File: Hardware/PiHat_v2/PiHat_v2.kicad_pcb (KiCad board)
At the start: 2 copper layers, 64 x 55 mm, 0 parts

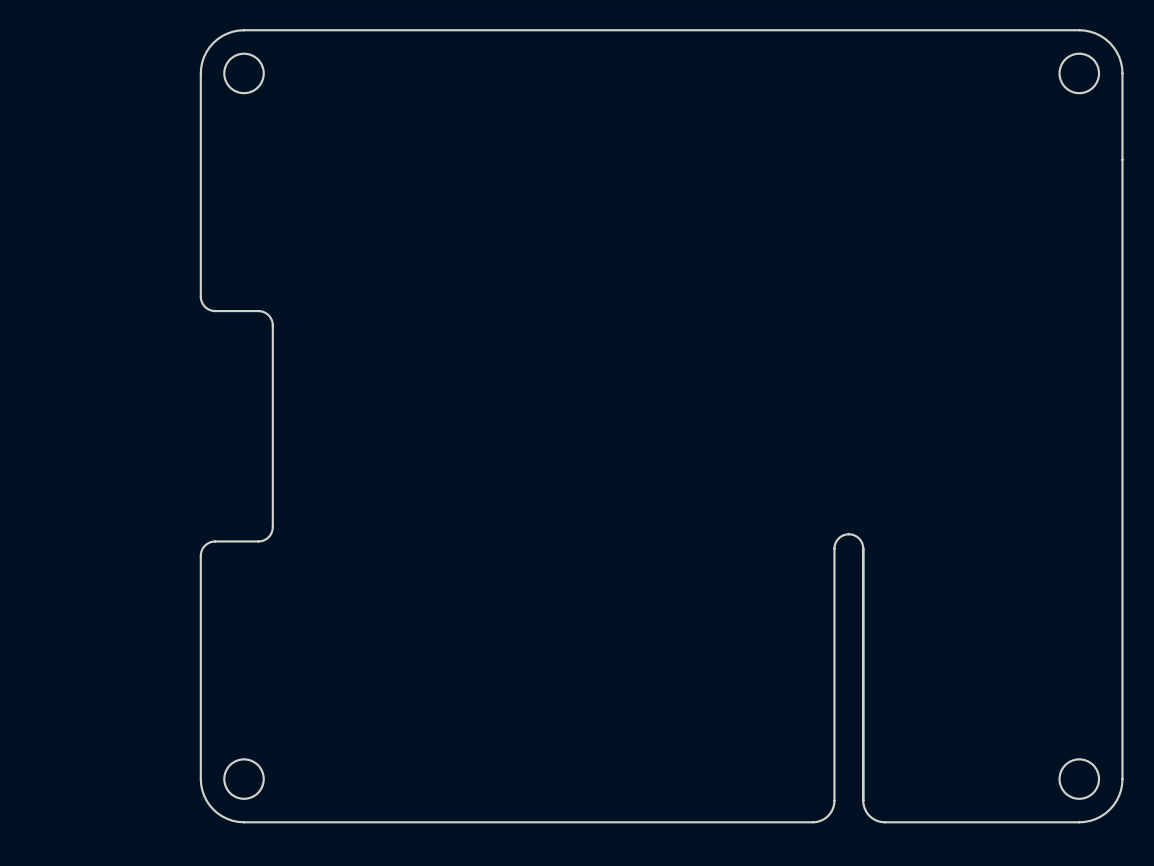
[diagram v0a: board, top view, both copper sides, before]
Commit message: Correct EEPROM Schematic - Add Pin Numbers
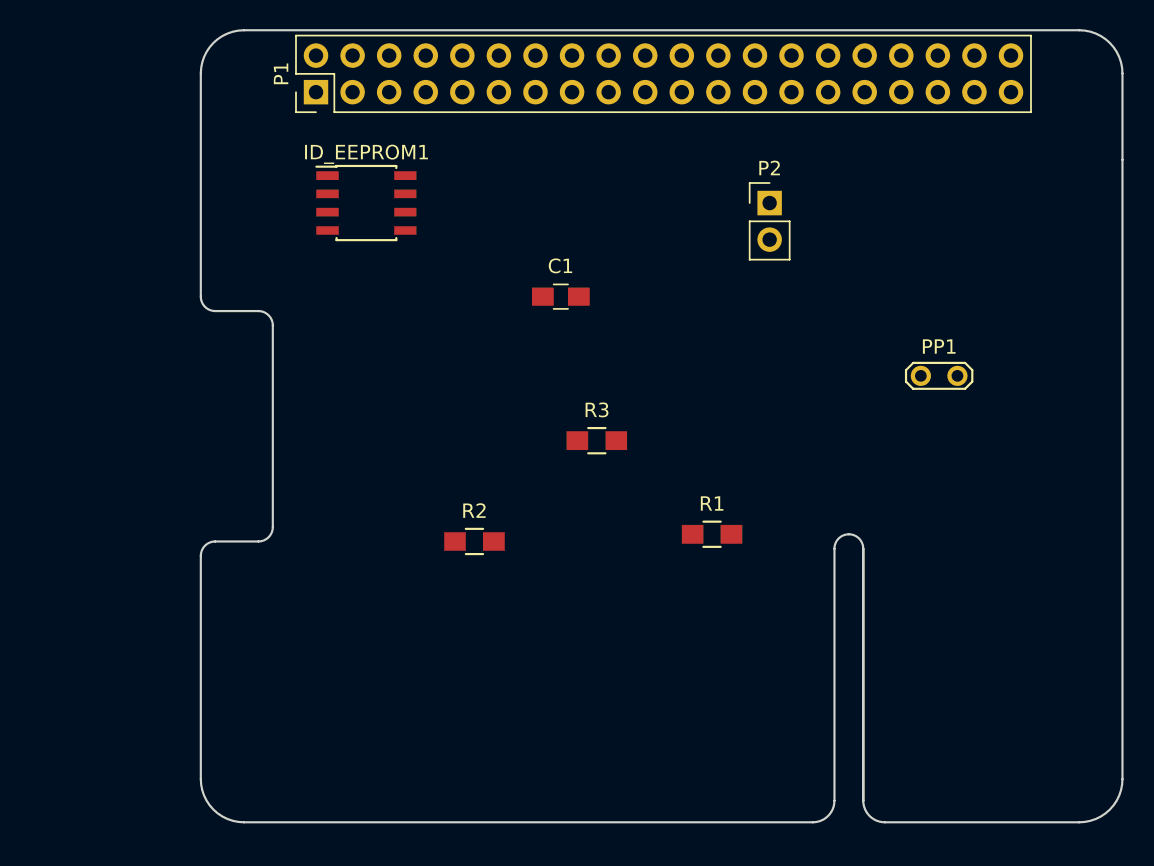
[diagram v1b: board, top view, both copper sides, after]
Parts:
- added C1: 100n, Capacitors_SMD:C_0805_HandSoldering, F.Cu at (119.0, 80.5)
- added ID_EEPROM1: CAT24C32, Housings_SOIC:SOIC-8_3.9x4.9mm_Pitch1.27mm, F.Cu at (105.5, 74.0)
- added P1: CONN_02X20, Pin_Headers:Pin_Header_Straight_2x20_Pitch2.54mm, F.Cu at (102.0, 66.3)
- added P2: CONN_01X02, Pin_Headers:Pin_Header_Straight_1x02_Pitch2.54mm, F.Cu at (133.5, 74.0)
- added PP1: horizTest, Measurement_Points:Test_Point_2Pads, F.Cu at (144.0, 86.0)
- added R1: 1K, Resistors_SMD:R_0805_HandSoldering, F.Cu at (129.5, 97.0)
- added R2: 3.9K, Resistors_SMD:R_0805_HandSoldering, F.Cu at (113.0, 97.5)
- added R3: 3.9K, Resistors_SMD:R_0805_HandSoldering, F.Cu at (121.5, 90.5)
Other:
- outline, holes or cut-outs redrawn

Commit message: Rough Sketch of Schematic and all Footprints Complete
* I've completed a first draft of the schematic, and verified that all
parts have a footprint.
* Next steps include routing the PCB, verifying the designs, and
including any changes.
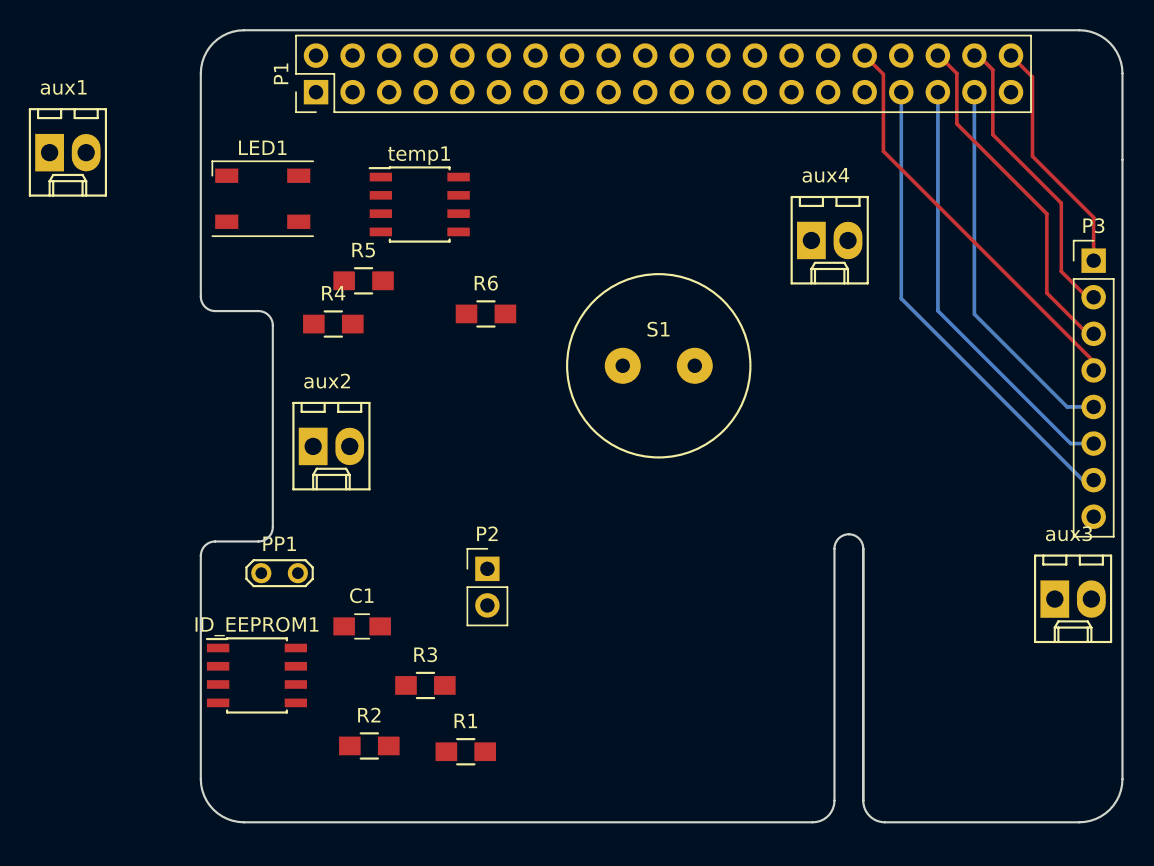
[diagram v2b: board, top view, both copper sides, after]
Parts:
- added LED1: Led_RGB_CA, LEDs:LED_Cree-PLCC4, F.Cu at (98.3, 73.7)
- added P3: CONN_01X08, Pin_Headers:Pin_Header_Straight_1x08_Pitch2.54mm, F.Cu at (156.0, 78.0)
- added R4: R, Resistors_SMD:R_0805_HandSoldering, F.Cu at (103.2, 82.4)
- added R5: R, Resistors_SMD:R_0805_HandSoldering, F.Cu at (105.3, 79.4)
- added R6: R, Resistors_SMD:R_0805_HandSoldering, F.Cu at (113.8, 81.7)
- added S1: Piezo, .pretty:PKM13EPYH, F.Cu at (125.8, 85.3)
- added aux1: CONN_01X02, Connectors_Molex:Molex_KK-6410-02_02x2.54mm_Straight, F.Cu at (83.5, 70.5)
- added aux2: CONN_01X02, Connectors_Molex:Molex_KK-6410-02_02x2.54mm_Straight, F.Cu at (101.8, 90.9)
- added aux3: CONN_01X02, Connectors_Molex:Molex_KK-6410-02_02x2.54mm_Straight, F.Cu at (153.3, 101.5)
- added aux4: CONN_01X02, Connectors_Molex:Molex_KK-6410-02_02x2.54mm_Straight, F.Cu at (136.4, 76.6)
- added temp1: LM75BD, Housings_SOIC:SOIC-8_3.9x4.9mm_Pitch1.27mm, F.Cu at (109.2, 74.1)
- moved PP1 47.8 mm to (98.2, 99.7)
- moved ID_EEPROM1 33.7 mm to (97.9, 106.8)
- moved P2 32.1 mm to (113.9, 99.4)
- moved C1 26.7 mm to (105.2, 103.4)
- moved R1 22.8 mm to (112.4, 112.1)
- moved R3 20.8 mm to (109.6, 107.5)
- moved R2 16.0 mm to (105.7, 111.7)
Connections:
- ID_EEPROM1 pad 1: (no net) -> GND
- ID_EEPROM1 pad 2: (no net) -> GND
- ID_EEPROM1 pad 3: (no net) -> GND
- ID_EEPROM1 pad 4: (no net) -> GND
- ID_EEPROM1 pad 5: (no net) -> /ID_SD
- ID_EEPROM1 pad 6: (no net) -> /ID_SC
- ID_EEPROM1 pad 7: (no net) -> Net-(ID_EEPROM1-Pad7)
- ID_EEPROM1 pad 8: (no net) -> +3V3
- P2 pad 1: Net-(ID_EEPROM1-Pad~) -> Net-(ID_EEPROM1-Pad7)
- PP1 pad 2: Net-(ID_EEPROM1-Pad~) -> Net-(ID_EEPROM1-Pad7)
- R1 pad 2: Net-(ID_EEPROM1-Pad~) -> Net-(ID_EEPROM1-Pad7)
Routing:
- net /GPIO13: track 0.00 -> 32.9 mm
- net /GPIO19: track 0.00 -> 29.8 mm
- net /GPIO12: track 0.00 -> 28.4 mm
- net /GPIO26: track 0.00 -> 26.4 mm
- net /GPIO16: track 0.00 -> 24.1 mm
- net /GPIO20: track 0.00 -> 20.6 mm
- net /GPIO21: track 0.00 -> 16.6 mm

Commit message: Complete First Draft of Routing
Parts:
- moved ID_EEPROM1 50.0 mm to (147.6, 112.4), turned to 90 degrees
- moved PP1 46.8 mm to (142.5, 114.9), turned to 90 degrees
- moved R2 43.4 mm to (148.7, 105.7), turned to 270 degrees
- moved R3 41.2 mm to (150.8, 105.7), turned to 270 degrees
- moved temp1 40.9 mm to (121.2, 113.2)
- moved C1 39.4 mm to (144.5, 105.7), turned to 270 degrees
- moved R1 34.8 mm to (146.6, 105.7), turned to 270 degrees
- moved aux1 32.7 mm to (116.2, 72.2), turned to 180 degrees
- moved S1 30.9 mm to (107.1, 109.9), turned to 180 degrees
- moved P2 29.1 mm to (142.0, 106.8)
- moved aux3 21.7 mm to (134.6, 112.5), turned to 180 degrees
- moved aux4 12.1 mm to (147.9, 73.0), turned to 180 degrees
- moved aux2 11.9 mm to (96.7, 101.7)
- moved R4 11.8 mm to (106.7, 71.1)
- moved R6 10.8 mm to (106.7, 73.5)
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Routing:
- net GND: track 0.00 -> 159.1 mm, vias 0 -> 2
- net +3V3: track 0.00 -> 122.9 mm, vias 0 -> 2
- net /GPIO7: track 0.00 -> 94.5 mm
- net /GPIO5: track 0.00 -> 67.0 mm
- net /ID_SC: track 0.00 -> 65.0 mm
- net /GPIO3: track 0.00 -> 64.8 mm, vias 0 -> 1
- net /GPIO2: track 0.00 -> 58.3 mm, vias 0 -> 1
- net /ID_SD: track 0.00 -> 54.4 mm
- net /GPIO17: track 0.00 -> 44.3 mm
- net /GPIO15: track 0.00 -> 15.2 mm
- net Net-(ID_EEPROM1-Pad7): track 0.00 -> 14.9 mm
- net /GPIO6: track 0.00 -> 11.0 mm
- net /GPIO18: track 0.00 -> 10.2 mm
- net Net-(LED1-Pad4): track 0.00 -> 9.94 mm
- net /GPIO4: track 0.00 -> 8.47 mm
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- added copper zone on B.Cu, net GND
